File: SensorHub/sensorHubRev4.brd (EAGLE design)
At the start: 80 x 80 mm, 71 parts, among them IC1 ADP3338AKCZ-3.3, IC2 FT231XQ, U2 TPS2065DBVR, U3 BS138PS, X1 32.768k, X2 332-02, X3 332-02

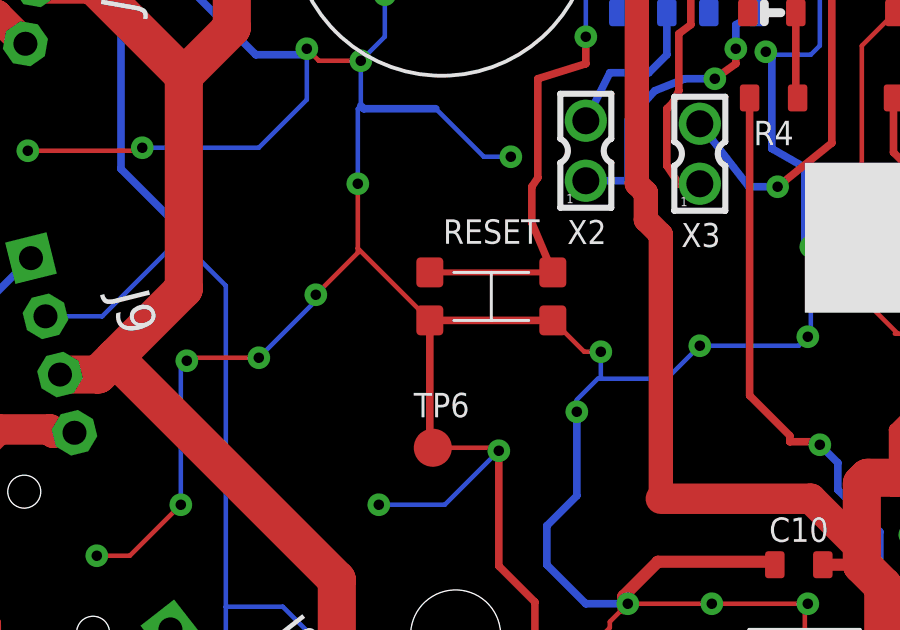
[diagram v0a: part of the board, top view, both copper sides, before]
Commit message: SensorHub
Botton position change.
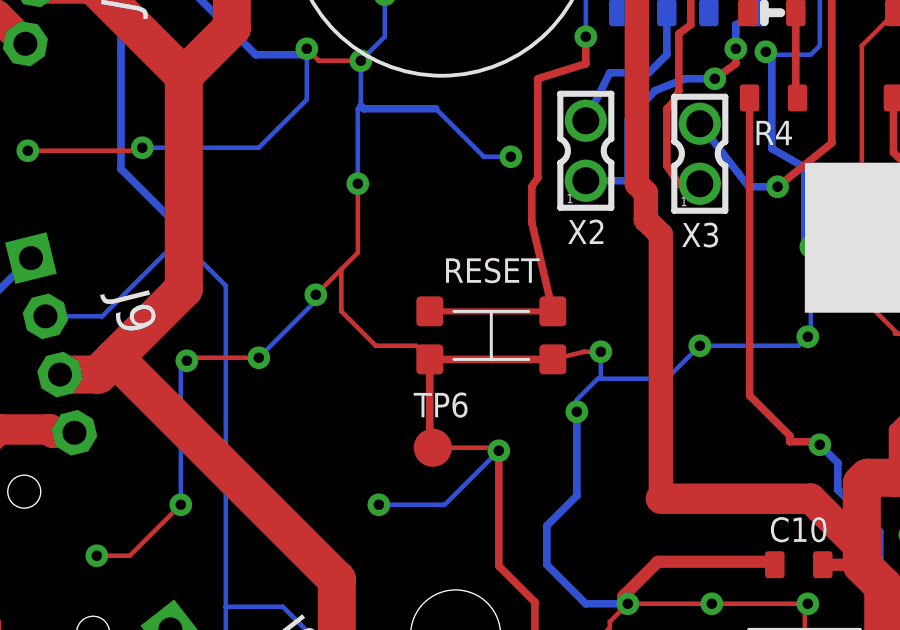
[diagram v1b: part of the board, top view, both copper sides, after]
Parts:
- moved RESET 1.30 mm to (24.1, 32.8)
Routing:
- net EN: track 82.8 -> 84.0 mm
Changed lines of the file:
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@@
 <attribute name="VALUE" x="33.46" y="40.76" size="1.016" layer="27" font="vector" ratio="15" align="center"/>
 </element>
-<element name="RESET" library="component" package="KMR2-TACT" value="" x="24.05" y="34.145" smashed="yes" rot="R180">
-<attribute name="NAME" x="24.05" y="35.899" size="0.8128" layer="25" font="vector" ratio="15" align="bottom-center"/>
+<element name="RESET" library="component" package="KMR2-TACT" value="" x="24.05" y="32.845" smashed="yes" rot="R180">
+<attribute name="NAME" x="24.05" y="34.599" size="0.8128" layer="25" font="vector" ratio="15" align="bottom-center"/>
 </element>
 <element name="BOOT" library="component" package="KMR2-TACT" value="" x="54.46" y="32.845" smashed="yes">
@@
 <wire x1="29.45" y1="18.95" x2="28.55" y2="18.95" width="0.8128" layer="1"/>
 <wire x1="22.1" y1="29.1" x2="22" y2="29.2" width="0.254" layer="1"/>
-<wire x1="22" y1="29.2" x2="22" y2="33.345" width="0.254" layer="1"/>
-<wire x1="22" y1="33.345" x2="26.1" y2="33.345" width="0.254" layer="1"/>
+<wire x1="22" y1="29.2" x2="22" y2="32.045" width="0.254" layer="1"/>
+<wire x1="22" y1="32.045" x2="26.1" y2="32.045" width="0.254" layer="1"/>
 <wire x1="48.405" y1="71.385" x2="42.9" y2="71.385" width="0.8128" layer="1"/>
 <wire x1="42.9" y1="71.385" x2="40.5" y2="71.385" width="0.8128" layer="1"/>
@@
 <via x="49.3" y="39.4" extent="1-16" drill="0.35"/>
 <wire x1="49.3" y1="39.4" x2="55.5" y2="39.4" width="0.1524" layer="16"/>
-<wire x1="22" y1="33.345" x2="19.6" y2="35.745" width="0.1524" layer="1"/>
 <via x="19.6" y="37.9" extent="1-16" drill="0.35"/>
-<wire x1="19.6" y1="35.745" x2="19.6" y2="37.9" width="0.1524" layer="1"/>
+<wire x1="19.6" y1="35.6" x2="19.6" y2="37.9" width="0.1524" layer="1"/>
 <wire x1="19.6" y1="37.9" x2="19.6" y2="40.4" width="0.1524" layer="16"/>
 <wire x1="36.405" y1="2.72" x2="35.6" y2="3.525" width="0.1524" layer="1"/>
@@
 <wire x1="27.6" y1="31.4" x2="26.9" y2="30.7" width="0.1524" layer="16"/>
 <wire x1="26.9" y1="30.7" x2="26.9" y2="30.3" width="0.1524" layer="16"/>
-<wire x1="26.1" y1="33.345" x2="27.145" y2="32.3" width="0.1524" layer="1"/>
+<wire x1="26.1" y1="32.045" x2="27.145" y2="32.3" width="0.1524" layer="1"/>
 <wire x1="27.145" y1="32.3" x2="27.7" y2="32.3" width="0.1524" layer="1"/>
 <via x="27.7" y="32.3" extent="1-16" drill="0.35"/>
@@
 <wire x1="24.3" y1="29" x2="24.2" y2="29.1" width="0.1524" layer="1"/>
 <wire x1="24.2" y1="29.1" x2="22.1" y2="29.1" width="0.1524" layer="1"/>
-<wire x1="18.2" y1="34.2" x2="19.6" y2="35.6" width="0.1524" layer="1"/>
-<wire x1="19.6" y1="35.6" x2="19.6" y2="35.745" width="0.1524" layer="1"/>
+<wire x1="18.2" y1="34.2" x2="19.05" y2="35.05" width="0.1524" layer="1"/>
+<wire x1="19.05" y1="35.05" x2="19.6" y2="35.6" width="0.1524" layer="1"/>
 <wire x1="17.9" y1="42.4" x2="18.3" y2="42" width="0.1524" layer="1"/>
 <wire x1="18.3" y1="42" x2="19.7" y2="42" width="0.1524" layer="1"/>
@@
 <wire x1="27.8" y1="71.7" x2="29.03" y2="71.7" width="0.254" layer="1"/>
 <wire x1="29.03" y1="71.7" x2="29.21" y2="71.52" width="0.254" layer="1"/>
+<wire x1="22" y1="32.045" x2="21.545" y2="32.5" width="0.1524" layer="1"/>
+<wire x1="21.545" y1="32.5" x2="20.2" y2="32.5" width="0.1524" layer="1"/>
+<wire x1="20.2" y1="32.5" x2="19.05" y2="33.65" width="0.1524" layer="1"/>
+<wire x1="19.05" y1="33.65" x2="19.05" y2="35.05" width="0.1524" layer="1"/>
 </signal>
 <signal name="3V3">
@@
 <wire x1="43.18369375" y1="45.47" x2="41.8" y2="45.47" width="0.1524" layer="1"/>
 <wire x1="41.8" y1="45.47" x2="41.73" y2="45.47" width="0.1524" layer="1"/>
-<wire x1="22" y1="34.945" x2="26.1" y2="34.945" width="0.2032" layer="1"/>
-<wire x1="26.1" y1="34.945" x2="25.4" y2="36.6" width="0.254" layer="1"/>
+<wire x1="22" y1="33.645" x2="26.1" y2="33.645" width="0.2032" layer="1"/>
+<wire x1="26.1" y1="33.645" x2="25.4" y2="36.6" width="0.254" layer="1"/>
 <wire x1="25.4" y1="36.6" x2="25.4" y2="37.8" width="0.254" layer="1"/>
 <wire x1="25.4" y1="37.8" x2="25.6" y2="38.1" width="0.254" layer="1"/>
